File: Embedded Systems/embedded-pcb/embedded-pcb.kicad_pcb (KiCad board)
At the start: 2 copper layers, 8 parts

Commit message: feat: updated schematic
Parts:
- removed Servos1: Conn_01x06, Connector_PinSocket_2.54mm:PinSocket_1x06_P2.54mm_Vertical
- added J1: Servos, Connector_PinSocket_2.54mm:PinSocket_1x06_P2.54mm_Vertical, F.Cu at (119.5, 103.0)
- added R4: R, Resistor_THT:R_Axial_DIN0207_L6.3mm_D2.5mm_P10.16mm_Horizontal, F.Cu at (75.4, 67.5)
- added R4*1: R, Resistor_THT:R_Axial_DIN0207_L6.3mm_D2.5mm_P10.16mm_Horizontal, F.Cu at (75.4, 83.8)
- added R5: R, Resistor_THT:R_Axial_DIN0207_L6.3mm_D2.5mm_P10.16mm_Horizontal, F.Cu at (75.4, 71.6)
- added R5*1: R, Resistor_THT:R_Axial_DIN0207_L6.3mm_D2.5mm_P10.16mm_Horizontal, F.Cu at (75.4, 87.8)
- added R7: R, Resistor_THT:R_Axial_DIN0207_L6.3mm_D2.5mm_P10.16mm_Horizontal, F.Cu at (75.4, 75.7)
- added R7*1: R, Resistor_THT:R_Axial_DIN0207_L6.3mm_D2.5mm_P10.16mm_Horizontal, F.Cu at (75.4, 91.8)
- added R8: R, Resistor_THT:R_Axial_DIN0207_L6.3mm_D2.5mm_P10.16mm_Horizontal, F.Cu at (75.4, 79.7)
- added R8*1: R, Resistor_THT:R_Axial_DIN0207_L6.3mm_D2.5mm_P10.16mm_Horizontal, F.Cu at (75.4, 95.9)
- added Rsen1: R, Resistor_THT:R_Axial_DIN0207_L6.3mm_D2.5mm_P10.16mm_Horizontal, F.Cu at (75.4, 100.0)
- added Rsen2: R, Resistor_THT:R_Axial_DIN0207_L6.3mm_D2.5mm_P10.16mm_Horizontal, F.Cu at (75.4, 104.0)
- added U1: LM324, Package_DIP:DIP-14_W7.62mm, F.Cu at (98.9, 112.4)
- added U2: LM324, Package_DIP:DIP-14_W7.62mm, F.Cu at (110.9, 111.0)
- D1: value Fault LED -> LED; footprint LED_THT:LED_D5.0mm_Horizontal_O1.27mm_Z9.0mm -> LED_THT:LED_D5.0mm
- D2: value Indicator LED -> LED; footprint LED_THT:LED_D5.0mm_Horizontal_O1.27mm_Z9.0mm -> LED_THT:LED_D5.0mm
- R2: value 160 -> 200
- RV1, RV2: value R_Potentiometer_Trim -> 10k; footprint Potentiometer_THT:Potentiometer_ACP_CA9-H2,5_Horizontal -> Potentiometer_THT:Potentiometer_Alps_RK163_Single_Horizontal
- moved RV2 89.6 mm to (152.0, 82.5)
- moved D1 83.7 mm to (148.5, 95.2)
- moved D2 79.6 mm to (148.5, 91.3), turned to 90 degrees
- moved RV1 78.8 mm to (152.0, 64.0)
- moved R1 59.8 mm to (122.5, 93.1)
- moved R2 57.5 mm to (126.5, 93.2)
- moved A1 47.1 mm to (133.7, 92.7)
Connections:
- A1 pad 17: unconnected-(A1-3V3-Pad17) -> Net-(A1-3V3)
- A1 pad 21: unconnected-(A1-A2-Pad21) -> Net-(A1-A2)
- A1 pad 22: unconnected-(A1-A3-Pad22) -> Net-(A1-A3)
- A1 pad 27: /Vcc -> Net-(A1-+5V)
- D1 pad 1: /GND -> Net-(D1-K)
- D1 pad 2: Net-(D1-A) -> Net-(A1-D9)
- D2 pad 1: /GND -> Net-(D2-K)
- D2 pad 2: Net-(D2-A) -> Net-(A1-D10)
- R1 pad 1: Net-(D1-A) -> Net-(D1-K)
- R1 pad 2: Net-(A1-D10) -> /GND
- R2 pad 1: Net-(D2-A) -> Net-(D2-K)
- R2 pad 2: Net-(A1-D9) -> /GND
- RV1 pad 1: /GND -> Net-(A1-3V3)
- RV1 pad 3: /Vcc -> /GND
- RV2 pad 1: /GND -> Net-(A1-3V3)
- RV2 pad 3: /Vcc -> /GND
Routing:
- net /PWM: track 74.2 -> 0.00 mm
- net /Vcc: track 56.3 -> 0.00 mm
- net Net-(A1-3V3): track 0.00 -> 55.3 mm
- net Net-(D2-A): track 36.7 -> 0.00 mm
- net Net-(A1-D9): track 3.16 -> 39.2 mm
- net Net-(D1-A): track 31.1 -> 0.00 mm
- net Net-(D1-K): track 0.00 -> 26.9 mm
- net Net-(A1-D10): track 7.65 -> 32.7 mm
- net Net-(D2-K): track 0.00 -> 22.8 mm
- net Net-(A1-A1): track 14.7 -> 0.00 mm
- net Net-(A1-A0): track 9.92 -> 0.00 mm
- net /GND: track 84.5 -> 85.5 mm

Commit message: feat: updated schematic
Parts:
- removed R7, R8: R, Resistor_THT:R_Axial_DIN0207_L6.3mm_D2.5mm_P10.16mm_Horizontal
- removed U2: LM324, Package_DIP:DIP-14_W7.62mm
- added R3: 1k, Resistor_THT:R_Axial_DIN0207_L6.3mm_D2.5mm_P10.16mm_Horizontal, F.Cu at (108.9, 63.4)
- added R6: 43, Resistor_THT:R_Axial_DIN0207_L6.3mm_D2.5mm_P10.16mm_Horizontal, F.Cu at (169.5, 99.5)
- R1, R2: value 200 -> 220
- R4, R5*1, R8*1: value R -> 1k
- R4*1, R7*1: value R -> 220
- R5: value R -> 43
- Rsen1, Rsen2: value R -> 10k
- moved R5 96.3 mm to (169.6, 92.0), turned to 180 degrees
- moved J1 91.1 mm to (174.5, 30.5), turned to 0 degrees
- moved U1 81.5 mm to (136.0, 39.8)
- moved R1 40.2 mm to (108.9, 55.3), turned to 0 degrees
- moved R2 38.1 mm to (108.9, 59.4), turned to 0 degrees
- moved R4*1 33.7 mm to (108.9, 79.6)
- moved R8*1 33.7 mm to (108.9, 91.8)
- moved Rsen1 33.7 mm to (108.9, 95.8)
- moved Rsen2 33.7 mm to (108.9, 99.8)
- moved R5*1 33.7 mm to (108.9, 83.7)
- moved R7*1 33.7 mm to (108.9, 87.7)
- moved R4 33.4 mm to (108.9, 67.5)
- moved D2 29.2 mm to (176.5, 99.7), turned to -90 degrees
- moved D1 28.2 mm to (176.5, 92.2)
- moved RV1 28.1 mm to (180.0, 62.0)
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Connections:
- R1 pad 1: Net-(D1-K) -> Net-(A1-+5V)
- R1 pad 2: /GND -> Net-(U1A-+)
- R2 pad 1: Net-(D2-K) -> Net-(A1-+5V)
- R2 pad 2: /GND -> Net-(U1B-+)
- R4 pad 1: Net-(A1-+5V) -> Net-(U1B-+)
- R4 pad 2: Net-(U1A-+) -> /GND
- R5 pad 1: Net-(U1A-+) -> Net-(D1-K)
- R7*1 pad 2: Net-(U2A--) -> Net-(U1B--)
- R8*1 pad 1: Net-(U2A--) -> Net-(U1B--)
- U1 pad 11: (no net) -> /GND
- U1 pad 4: (no net) -> Net-(A1-+5V)
- U1 pad 5: (no net) -> Net-(U1B-+)
- U1 pad 6: (no net) -> Net-(U1B--)
- U1 pad 7: (no net) -> Net-(A1-A2)
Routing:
- net /PWM: track 0.00 -> 153.1 mm
- net Net-(A1-A1): track 0.00 -> 63.3 mm
- net Net-(A1-A0): track 0.00 -> 41.0 mm
- net /GND: track 85.5 -> 110.8 mm
- net Net-(D1-K): track 26.9 -> 7.33 mm
- net Net-(D2-K): track 22.8 -> 7.41 mm
- net Net-(A1-3V3): track 55.3 -> 67.2 mm
- net Net-(A1-D10): track 32.7 -> 38.4 mm

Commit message: feat: updated schematic
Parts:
- moved Rsen1 94.8 mm to (169.0, 22.6), turned to -90 degrees
- moved Rsen2 77.8 mm to (169.0, 50.5), turned to 90 degrees
- moved R7*1 74.2 mm to (166.0, 40.3), turned to 180 degrees
- moved R4*1 73.9 mm to (166.0, 32.7), turned to 180 degrees
- moved R1 65.9 mm to (166.0, 22.6), turned to 180 degrees
- moved R2 57.8 mm to (166.0, 50.5), turned to 180 degrees
- moved R3 25.3 mm to (132.5, 54.4), turned to -90 degrees
- moved R4 24.0 mm to (129.0, 54.4), turned to -90 degrees
- moved U1 23.6 mm to (154.5, 54.5), turned to -90 degrees
- moved J1 0.28 mm to (174.5, 30.2)
- moved A1 0.05 mm to (139.3, 69.1)
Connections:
- R1 pad 2: Net-(U1A-+) -> Net-(U1B-+)
- R2 pad 2: Net-(U1B-+) -> Net-(U1A-+)
- R3 pad 1: Net-(U1A-+) -> Net-(U1B-+)
- R4 pad 1: Net-(U1B-+) -> Net-(U1A-+)
- R4*1 pad 2: Net-(U1A--) -> Net-(U1B--)
- R5*1 pad 1: Net-(U1A--) -> Net-(U1B--)
- R7*1 pad 2: Net-(U1B--) -> Net-(U1A--)
- R8*1 pad 1: Net-(U1B--) -> Net-(U1A--)
- U1 pad 1: Net-(A1-A3) -> Net-(A1-A2)
- U1 pad 7: Net-(A1-A2) -> Net-(A1-A3)
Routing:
- net Net-(A1-+5V): track 0.00 -> 88.7 mm
- net Net-(U1B-+): track 0.00 -> 40.0 mm
- net /GND: track 110.8 -> 144.7 mm
- net Net-(U1B--): track 0.00 -> 30.9 mm
- net Net-(U1A--): track 0.00 -> 17.8 mm
- net /Vcc: track 0.00 -> 17.0 mm
- net Net-(U1A-+): track 0.00 -> 8.04 mm

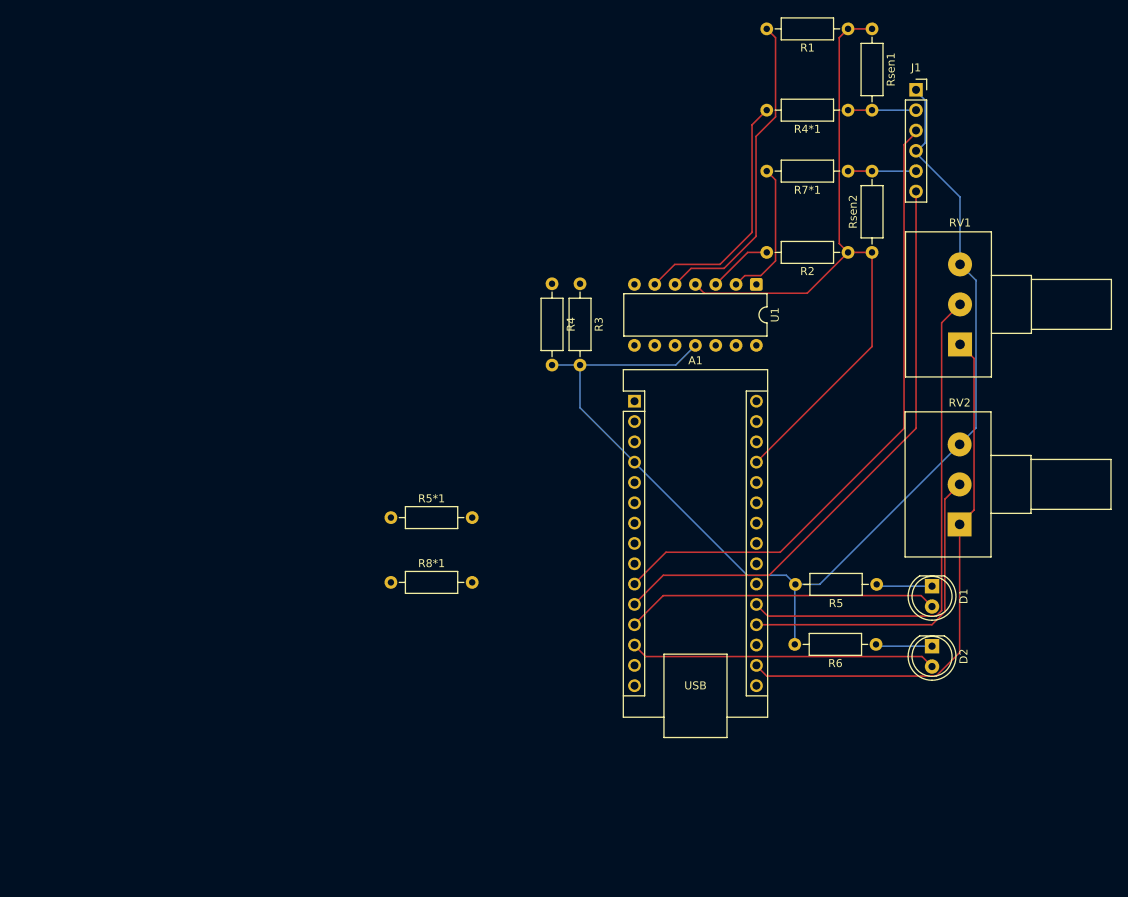
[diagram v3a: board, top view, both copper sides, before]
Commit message: feat: v2 of PCB design
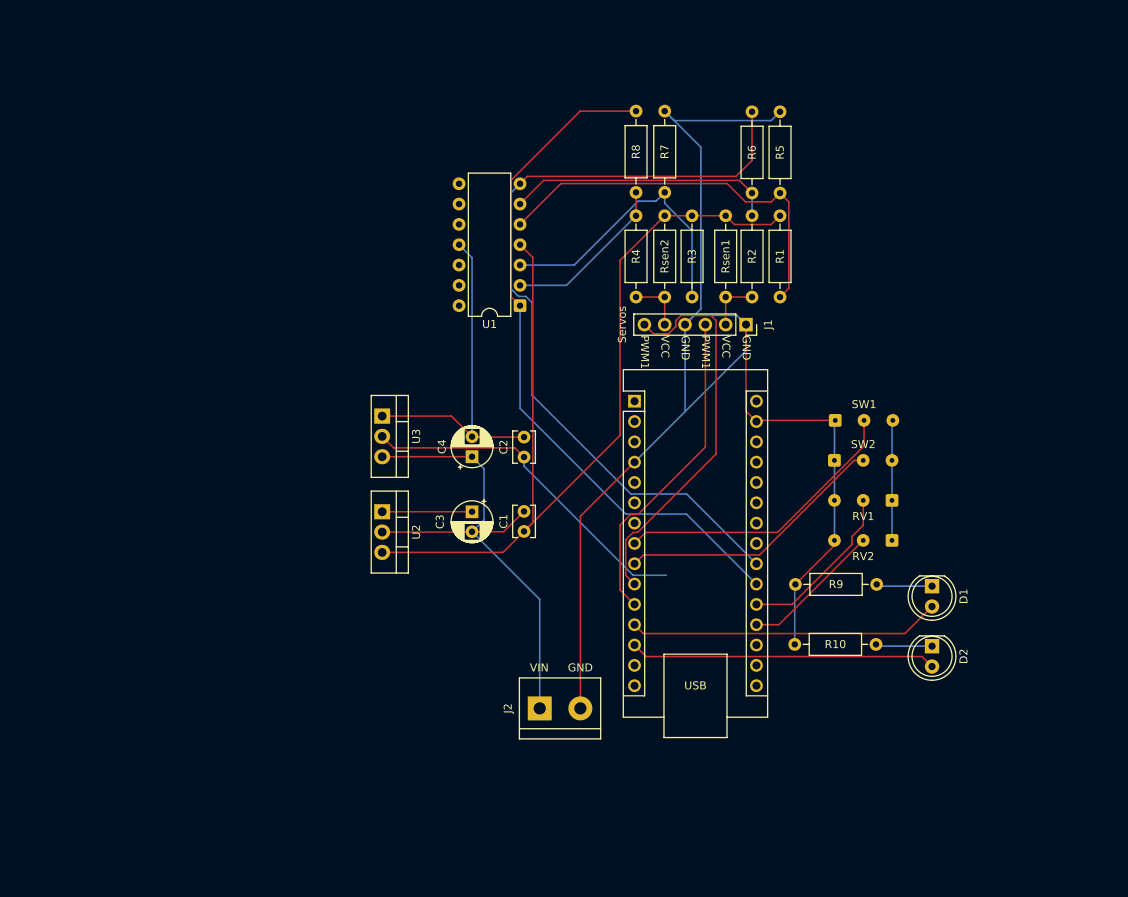
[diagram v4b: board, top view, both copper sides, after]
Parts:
- removed R4*1, R7*1: 220, Resistor_THT:R_Axial_DIN0207_L6.3mm_D2.5mm_P10.16mm_Horizontal
- removed R5*1, R8*1: 1k, Resistor_THT:R_Axial_DIN0207_L6.3mm_D2.5mm_P10.16mm_Horizontal
- added C1: C, Capacitor_THT:C_Disc_D3.8mm_W2.6mm_P2.50mm, F.Cu at (125.5, 85.4)
- added C2: C, Capacitor_THT:C_Disc_D3.8mm_W2.6mm_P2.50mm, F.Cu at (125.5, 76.1)
- added C3: C_Polarized, Capacitor_THT:CP_Radial_D5.0mm_P2.50mm, F.Cu at (119.0, 82.9)
- added C4: C_Polarized, Capacitor_THT:CP_Radial_D5.0mm_P2.50mm, F.Cu at (119.0, 76.0)
- added J2: Screw_Terminal_01x02, TerminalBlock:TerminalBlock_bornier-2_P5.08mm, F.Cu at (127.5, 107.5)
- added R5: 1k, Resistor_THT:R_Axial_DIN0207_L6.3mm_D2.5mm_P10.16mm_Horizontal, F.Cu at (157.5, 43.1)
- added R6: 1k, Resistor_THT:R_Axial_DIN0207_L6.3mm_D2.5mm_P10.16mm_Horizontal, F.Cu at (154.0, 43.1)
- added R7: 1k, Resistor_THT:R_Axial_DIN0207_L6.3mm_D2.5mm_P10.16mm_Horizontal, F.Cu at (143.1, 43.0)
- added R8: 1k, Resistor_THT:R_Axial_DIN0207_L6.3mm_D2.5mm_P10.16mm_Horizontal, F.Cu at (139.5, 43.0)
- added SW1: SW_SPDT, Connector_Wire:SolderWire-0.1sqmm_1x03_P3.6mm_D0.4mm_OD1mm, F.Cu at (164.4, 71.5)
- added SW2: SW_SPDT, Connector_Wire:SolderWire-0.1sqmm_1x03_P3.6mm_D0.4mm_OD1mm, F.Cu at (164.3, 76.5)
- added U2: LM7805_TO220, Package_TO_SOT_THT:TO-220-3_Vertical, F.Cu at (107.8, 82.9)
- added U3: LM1117T-3.3, Package_TO_SOT_THT:TO-220-3_Vertical, F.Cu at (107.8, 71.0)
- R10: renamed from R6; value 43 -> 47
- R3, R4: value 1k -> 220
- R9: renamed from R5; value 43 -> 47
- RV1, RV2: footprint Potentiometer_THT:Potentiometer_Alps_RK163_Single_Horizontal -> Connector_Wire:SolderWire-0.1sqmm_1x03_P3.6mm_D0.4mm_OD1mm
- moved J1 36.2 mm to (153.2, 59.5), turned to -90 degrees
- moved Rsen1 29.7 mm to (150.7, 45.9)
- moved U1 29.7 mm to (125.0, 57.2), turned to 180 degrees
- moved Rsen2 26.3 mm to (143.1, 45.9), turned to -90 degrees
- moved R1 24.9 mm to (157.5, 45.9), turned to -90 degrees
- moved RV1 21.3 mm to (171.5, 81.5)
- moved R3 16.4 mm to (146.5, 45.9)
- moved R2 13.2 mm to (154.0, 56.1), turned to 90 degrees
- moved R4 10.6 mm to (139.5, 56.1), turned to 90 degrees
- moved RV2 8.68 mm to (171.5, 86.5)
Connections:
- net Net-(A1-3V3) renamed /Power Management/+3.3v
- A1 pad 27: Net-(A1-+5V) -> unconnected-(A1-+5V-Pad27)
- A1 pad 29: unconnected-(A1-GND-Pad29) -> /GND
- A1 pad 8: unconnected-(A1-D5-Pad8) -> Net-(A1-D5)
- A1 pad 9: unconnected-(A1-D6-Pad9) -> Net-(A1-D6)
- R1 pad 1: Net-(A1-+5V) -> /Power Management/+5v
- R2 pad 1: Net-(A1-+5V) -> /Vcc
- R2 pad 2: Net-(U1A-+) -> Net-(U1B--)
- R3 pad 1: Net-(U1B-+) -> /Power Management/+5v
- R3 pad 2: /GND -> Net-(U1A-+)
- R4 pad 1: Net-(U1A-+) -> /Vcc
- R4 pad 2: /GND -> Net-(U1A--)
- Rsen1 pad 1: Net-(A1-+5V) -> /Power Management/+5v
- Rsen2 pad 1: Net-(A1-+5V) -> /Power Management/+5v
- U1 pad 4: Net-(A1-+5V) -> /Power Management/+5v
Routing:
- net /GND: track 144.7 -> 294.9 mm
- net /Power Management/+5v: track 0.00 -> 117.8 mm
- net Net-(A1-A3): track 0.00 -> 101.6 mm
- net Net-(A1-+5V): track 88.7 -> 0.00 mm
- net Net-(A1-A2): track 0.00 -> 86.8 mm
- net /PWM: track 153.1 -> 90.2 mm
- net Net-(A1-A1): track 63.3 -> 21.1 mm
- net Net-(A1-D5): track 0.00 -> 36.9 mm
- net Net-(A1-D6): track 0.00 -> 33.9 mm
- net Net-(U1A-+): track 8.04 -> 36.3 mm
- net Net-(A1-A0): track 41.0 -> 17.7 mm
- net Net-(U1B-+): track 40.0 -> 49.9 mm
- net /Power Management/+3.3v: track 67.2 -> 58.4 mm
- net /Vcc: track 17.0 -> 13.8 mm
- net Net-(U1A--): track 17.8 -> 21.0 mm
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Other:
- board text added: "GND"
- board text added: "PWM1"
- board text added: "VCC"
- board text added: "VIN"

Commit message: feat: finalised PCB
Finalised the electrical design and PCB, including adding a power switch, silksreening, and mounting holes.
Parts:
- added REF**: MountingHole_2.2mm_M2_DIN965_Pad, MountingHole:MountingHole_2.2mm_M2_DIN965_Pad, F.Cu at (159.0, 61.8)
- added REF**: MountingHole_2.2mm_M2_DIN965_Pad, MountingHole:MountingHole_2.2mm_M2_DIN965_Pad, F.Cu at (118.5, 103.8)
- added REF**: MountingHole_2.2mm_M2_DIN965_Pad, MountingHole:MountingHole_2.2mm_M2_DIN965_Pad, F.Cu at (118.8, 36.2)
- added SW3: SW_SPDT, Connector_Wire:SolderWire-0.1sqmm_1x03_P3.6mm_D0.4mm_OD1mm, F.Cu at (127.5, 91.4)
- RV1, RV2: value 10k -> 1k
- moved R10 29.4 mm to (143.0, 86.9), turned to 90 degrees
- moved R9 23.9 mm to (146.2, 86.9), turned to 90 degrees
- moved D1 15.8 mm to (160.8, 93.1)
- moved D2 15.8 mm to (160.8, 99.5)
- moved C1 7.28 mm to (132.7, 84.4)
- moved U2 7.28 mm to (115.0, 82.0)
- moved C2 7.28 mm to (132.7, 75.1)
- moved U3 7.28 mm to (115.0, 70.0)
- moved C3 7.28 mm to (126.2, 82.0)
- moved C4 7.28 mm to (126.2, 75.1)
- moved U1 7.28 mm to (132.2, 56.2)
- moved RV2 5.66 mm to (165.8, 86.9)
- moved RV1 5.66 mm to (165.8, 81.8)
- moved SW2 5.65 mm to (158.7, 76.7)
- moved SW1 5.65 mm to (158.8, 71.6)
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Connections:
- J2 pad 1: /GND -> /Power Management/VIN
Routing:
- net /Power Management/+3.3v: track 58.4 -> 105.4 mm
- net /Power Management/+5v: track 117.8 -> 83.8 mm
- net Net-(A1-D10): track 38.3 -> 22.4 mm
- net Net-(A1-D9): track 39.0 -> 23.2 mm
- net Net-(D2-K): track 7.41 -> 23.0 mm
- net Net-(D1-K): track 7.33 -> 17.1 mm
- net Net-(A1-A3): track 101.6 -> 92.1 mm
- net Net-(A1-A2): track 86.8 -> 77.4 mm
- net Net-(U1B--): track 33.7 -> 26.1 mm
- net Net-(U1A-+): track 36.3 -> 28.7 mm
- net Net-(U1B-+): track 49.9 -> 42.3 mm
- net Net-(U1A--): track 21.0 -> 13.7 mm
- net /Power Management/VIN: track 0.00 -> 6.15 mm
- net Net-(A1-A1): track 21.1 -> 15.9 mm
- net /GND: track 294.9 -> 300.0 mm
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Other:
- board outline added: 54.5 x 77.5 mm
- board text added: "+3.3v"
- board text added: "Morphing Wing Control Board v1.0 JLCJLCJLCJLC"
- board text added: "OUT"
- board text added: "mvx01"
